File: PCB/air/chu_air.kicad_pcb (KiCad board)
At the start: 2 copper layers, 210 x 10 mm, 24 parts, among them J1 Conn_01x06_Socket, Q1 Q_Photo_NPN, Q2 Q_Photo_NPN, Q3 Q_Photo_NPN, Q4 Q_Photo_NPN, Q5 Q_Photo_NPN, Q6 Q_Photo_NPN

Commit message: Another attempt of chu air
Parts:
- removed D10, D11, D12, D4, D5, D6, D7, D8, D9: IR26-21C_L110_TR8, LED_SMD:LED_1206_3216Metric_Pad1.42x1.75mm_HandSolder
- added J2: Conn_01x06_Socket, chu_air:6P_Air_Conn, F.Cu at (48.6, 97.5)
- added R6: 1R, Resistor_SMD:R_0603_1608Metric, B.Cu at (212.6, 98.8)
- added R7: 10K, Resistor_SMD:R_0603_1608Metric, B.Cu at (249.6, 97.5)
- D1, D2, D3: footprint LED_SMD:LED_1206_3216Metric_Pad1.42x1.75mm_HandSolder -> LED_THT:LED_D5.0mm_IRGrey
- J1: moved to F.Cu
- Q1, Q3, Q5: value Q_Photo_NPN -> AO3400A; footprint LED_SMD:LED_1206_3216Metric_Pad1.42x1.75mm_HandSolder -> Package_TO_SOT_SMD:SOT-23
- Q2, Q4, Q6: footprint LED_SMD:LED_1206_3216Metric_Pad1.42x1.75mm_HandSolder -> LED_THT:LED_D5.0mm_IRBlack; moved to F.Cu
- R1, R3: value R -> 10R; footprint Resistor_SMD:R_0805_2012Metric_Pad1.20x1.40mm_HandSolder -> Resistor_SMD:R_0603_1608Metric; moved to B.Cu
- R2: value R -> 1R; footprint Resistor_SMD:R_0805_2012Metric_Pad1.20x1.40mm_HandSolder -> Resistor_SMD:R_0603_1608Metric; moved to B.Cu
- R4: value R -> 1R; footprint Resistor_SMD:R_0805_2012Metric_Pad1.20x1.40mm_HandSolder -> Resistor_SMD:R_0603_1608Metric
- R5: value R -> 10R; footprint Resistor_SMD:R_0805_2012Metric_Pad1.20x1.40mm_HandSolder -> Resistor_SMD:R_0603_1608Metric
- moved R4 99.4 mm to (140.6, 98.8), turned to 180 degrees
- moved R3 76.4 mm to (140.6, 96.2), turned to 0 degrees
- moved R2 76.4 mm to (68.6, 98.8), turned to 180 degrees
- moved D3 68.5 mm to (206.6, 98.8)
- moved D2 34.8 mm to (134.6, 98.8)
- moved R5 27.4 mm to (212.6, 96.2)
- moved Q1 9.63 mm to (74.6, 97.5), turned to 180 degrees
- moved Q3 9.63 mm to (146.6, 97.5), turned to 180 degrees
- moved Q5 9.63 mm to (218.6, 97.5), turned to 180 degrees
- moved R1 4.71 mm to (68.6, 96.2), turned to 0 degrees
- moved D1 3.74 mm to (62.6, 98.8)
- moved Q2 2.69 mm to (98.6, 96.2)
- moved Q4 2.69 mm to (170.6, 96.2)
- moved Q6 2.69 mm to (242.6, 96.2)
- moved J1 2.63 mm to (256.6, 97.5)
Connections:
- D1 pad 2: Net-(D1-A) -> +3.3V
- D2 pad 1: Net-(D1-A) -> Net-(D2-K)
- D2 pad 2: Net-(D2-A) -> +3.3V
- D3 pad 2: Net-(D3-A) -> +3.3V
- J1 pad 4: /AD2 -> +3.3V
- J1 pad 5: GND -> /SIG
- J1 pad 6: /AD1 -> GND
- Q1 pad 1: /A -> Net-(Q1-G)
- Q1 pad 2: /AD1 -> GND
- Q2 pad 1: /B -> /A
- Q2 pad 2: /AD1 -> /SIG
- Q3 pad 1: /C -> Net-(Q3-G)
- Q3 pad 2: /AD1 -> GND
- Q4 pad 1: /A -> /B
- Q4 pad 2: /AD2 -> /SIG
- Q5 pad 1: /B -> Net-(Q5-G)
- Q5 pad 2: /AD2 -> GND
- Q6 pad 2: /AD2 -> /SIG
- R1 pad 2: Net-(D1-A) -> Net-(Q1-G)
- R2 pad 1: /C -> Net-(Q1-D)
- R2 pad 2: Net-(D3-A) -> Net-(D1-K)
- R3 pad 2: Net-(D5-A) -> Net-(Q3-G)
- R4 pad 1: /AD1 -> Net-(Q3-D)
- R4 pad 2: GND -> Net-(D2-K)
- R5 pad 1: /AD2 -> /C
- R5 pad 2: GND -> Net-(Q5-G)
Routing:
- net /SIG: track 0.00 -> 228.1 mm, vias 0 -> 2
- net +3.3V: track 0.00 -> 217.0 mm
- net /AD1: track 196.5 -> 0.00 mm
- net GND: track 32.2 -> 219.0 mm, vias 0 -> 14
- net /C: track 132.8 -> 260.1 mm, vias 2 -> 0
- net /AD2: track 95.2 -> 0.00 mm
- net /B: track 206.9 -> 252.5 mm, vias 2 -> 1
- net Net-(D1-A): track 37.6 -> 0.00 mm
- net Net-(D3-A): track 36.8 -> 0.00 mm
- net Net-(D5-A): track 35.7 -> 0.00 mm
- net /A: track 253.4 -> 231.6 mm, vias 2 -> 0
- net Net-(Q1-G): track 0.00 -> 6.25 mm
- net Net-(Q5-G): track 0.00 -> 6.25 mm
- net Net-(Q3-G): track 0.00 -> 6.25 mm
- net Net-(D2-K): track 0.00 -> 5.18 mm
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- added copper zone on B.Cu, net GND
- added copper zone on F.Cu, net GND
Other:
- board size 210 x 10 mm -> 220 x 10.1 mm
- board text added: "Air v1.2"
- board text added: "C B A"
- board text added: "G S V"
- board text removed: "Air v1.1"

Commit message: Air PCB v1.3
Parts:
- added C1: 47uF, Capacitor_SMD:CP_Elec_5x5.9, F.Cu at (116.6, 97.5)
- added C2: 47uF, Capacitor_SMD:CP_Elec_5x5.9, F.Cu at (188.6, 97.5)
- added R10: 10K, Resistor_SMD:R_0603_1608Metric_Pad0.98x0.95mm_HandSolder, B.Cu at (249.6, 97.5)
- added R8: 2K, Resistor_SMD:R_0603_1608Metric_Pad0.98x0.95mm_HandSolder, B.Cu at (166.6, 97.5)
- added R9: 2K, Resistor_SMD:R_0603_1608Metric_Pad0.98x0.95mm_HandSolder, B.Cu at (238.6, 97.5)
- Q1, Q3, Q5: value AO3400A -> 2N7002
- R1, R2, R3, R4, R5, R6: footprint Resistor_SMD:R_0603_1608Metric -> Resistor_SMD:R_0603_1608Metric_Pad0.98x0.95mm_HandSolder
- R7: value 10K -> 2K; footprint Resistor_SMD:R_0603_1608Metric -> Resistor_SMD:R_0603_1608Metric_Pad0.98x0.95mm_HandSolder
- moved R7 155.0 mm to (94.6, 97.5), turned to -90 degrees
- moved Q1 3.00 mm to (71.6, 97.5)
- moved Q3 3.00 mm to (143.6, 97.5)
- moved Q5 3.00 mm to (215.6, 97.5)
- moved R1 2.00 mm to (66.6, 96.2)
- moved R2 2.00 mm to (66.6, 98.8)
- moved R3 2.00 mm to (138.6, 96.2)
- moved R4 2.00 mm to (138.6, 98.8)
- moved R5 2.00 mm to (210.6, 96.2)
- moved R6 2.00 mm to (210.6, 98.8)
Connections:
- R7 pad 1: /SIG -> /A
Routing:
- net +3.3V: track 217.0 -> 225.5 mm
- net /B: track 252.5 -> 257.1 mm
- net /C: track 260.1 -> 264.4 mm
- net /A: track 231.6 -> 235.7 mm
- net Net-(D3-K): track 5.18 -> 3.09 mm
- net Net-(D2-K): track 5.18 -> 3.09 mm
- net Net-(D1-K): track 5.18 -> 3.09 mm
- net Net-(Q1-G): track 6.25 -> 5.16 mm
- net Net-(Q1-D): track 4.76 -> 3.68 mm
- net Net-(Q3-D): track 4.76 -> 3.68 mm
- net Net-(Q5-G): track 6.25 -> 5.16 mm
- net Net-(Q5-D): track 4.76 -> 3.68 mm
- net Net-(Q3-G): track 6.25 -> 5.16 mm
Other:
- board text added: "A B C"
- board text added: "Air v1.3"
- board text added: "V S G"
- board text removed: "Air v1.2"

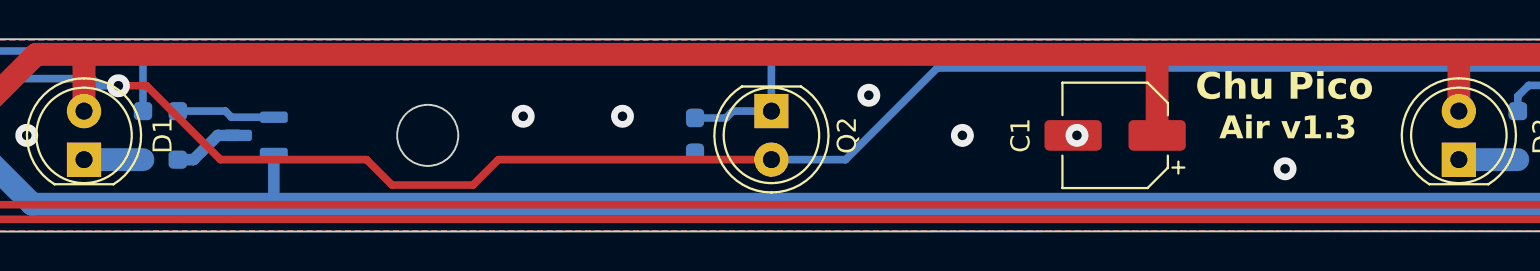
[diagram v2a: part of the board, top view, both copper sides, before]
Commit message: Air PCB v1.31 (update screw clearance)
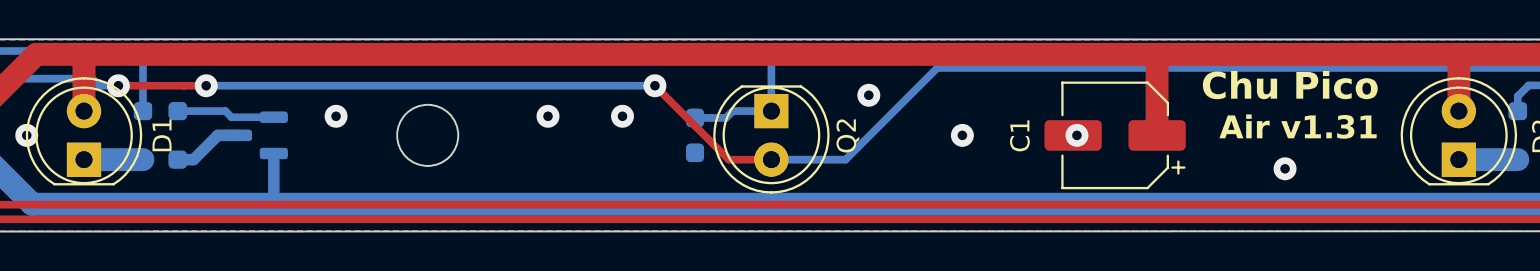
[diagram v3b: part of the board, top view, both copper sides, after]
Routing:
- net /SIG: track 228.0 -> 226.9 mm, vias 2 -> 4
- net GND: vias 14 -> 15
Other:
- board text added: "Air v1.31"
- board text removed: "Air v1.3"
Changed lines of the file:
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@@
 		)
 	)
-	(gr_text "Air v1.3"
+	(gr_text "Air v1.31"
 		(at 122.08 97.8 0)
 		(layer "F.SilkS")
@@
 	)
 	(gr_text "Chu Pico"
-		(at 120.83 95.75 0)
+		(at 121.13 95.75 0)
 		(layer "F.SilkS")
 		(effects
@@
 	)
 	(via
-		(at 85.63 96.5)
+		(at 86.93 96.5)
 		(size 1.2)
 		(drill 0.5)
@@
 	(via
 		(at 59.63 97.5)
+		(size 1.2)
+		(drill 0.5)
+		(layers "F.Cu" "B.Cu")
+		(net 4)
+	)
+	(via
+		(at 75.83 96.5)
 		(size 1.2)
 		(drill 0.5)
@@
 	)
 	(segment
+		(start 64.43 94.9)
+		(end 67.87 94.9)
+		(width 0.4)
+		(layer "F.Cu")
+		(net 8)
+	)
+	(segment
+		(start 67.87 94.9)
+		(end 69.03 94.9)
+		(width 0.4)
+		(layer "F.Cu")
+		(net 8)
+	)
+	(segment
+		(start 96.4 98.77)
+		(end 98.63 98.77)
+		(width 0.4)
+		(layer "F.Cu")
+		(net 8)
+	)
+	(segment
 		(start 53.316 97.5)
 		(end 49.9 97.5)
@@
 	)
 	(segment
-		(start 84.33 98.77)
-		(end 98.63 98.77)
-		(width 0.4)
-		(layer "F.Cu")
-		(net 8)
-	)
-	(segment
-		(start 78.76 100.1)
-		(end 83 100.1)
-		(width 0.4)
-		(layer "F.Cu")
-		(net 8)
-	)
-	(segment
-		(start 64.43 94.9)
-		(end 65.9052 94.9)
-		(width 0.4)
-		(layer "F.Cu")
-		(net 8)
-	)
-	(segment
 		(start 56.2878 94.5282)
 		(end 53.316 97.5)
@@
 	)
 	(segment
-		(start 77.43 98.77)
-		(end 78.76 100.1)
-		(width 0.4)
-		(layer "F.Cu")
-		(net 8)
-	)
-	(segment
-		(start 69.7752 98.77)
-		(end 77.43 98.77)
-		(width 0.4)
-		(layer "F.Cu")
-		(net 8)
-	)
-	(segment
-		(start 65.9052 94.9)
-		(end 69.7752 98.77)
-		(width 0.4)
-		(layer "F.Cu")
-		(net 8)
-	)
-	(segment
-		(start 83 100.1)
-		(end 84.33 98.77)
-		(width 0.4)
-		(layer "F.Cu")
+		(start 92.53 94.9)
+		(end 96.4 98.77)
+		(width 0.4)
+		(layer "F.Cu")
+		(net 8)
+	)
+	(via
+		(at 92.53 94.9)
+		(size 1.2)
+		(drill 0.5)
+		(layers "F.Cu" "B.Cu")
+		(net 8)
+	)
+	(via
+		(at 69.03 94.9)
+		(size 1.2)
+		(drill 0.5)
+		(layers "F.Cu" "B.Cu")
 		(net 8)
 	)
@@
 		(width 0.4)
 		(layer "B.Cu")
+		(net 8)
+	)
+	(segment
+		(start 69.03 94.9)
+		(end 92.53 94.9)
+		(width 0.4)
+		(layer "B.Cu")
